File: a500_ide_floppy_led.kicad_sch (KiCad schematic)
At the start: 6 parts, among them J1 Motherboard, J2 Keyboard, J3 ~{IDE_ACTIVITY}, Q1 2N3906

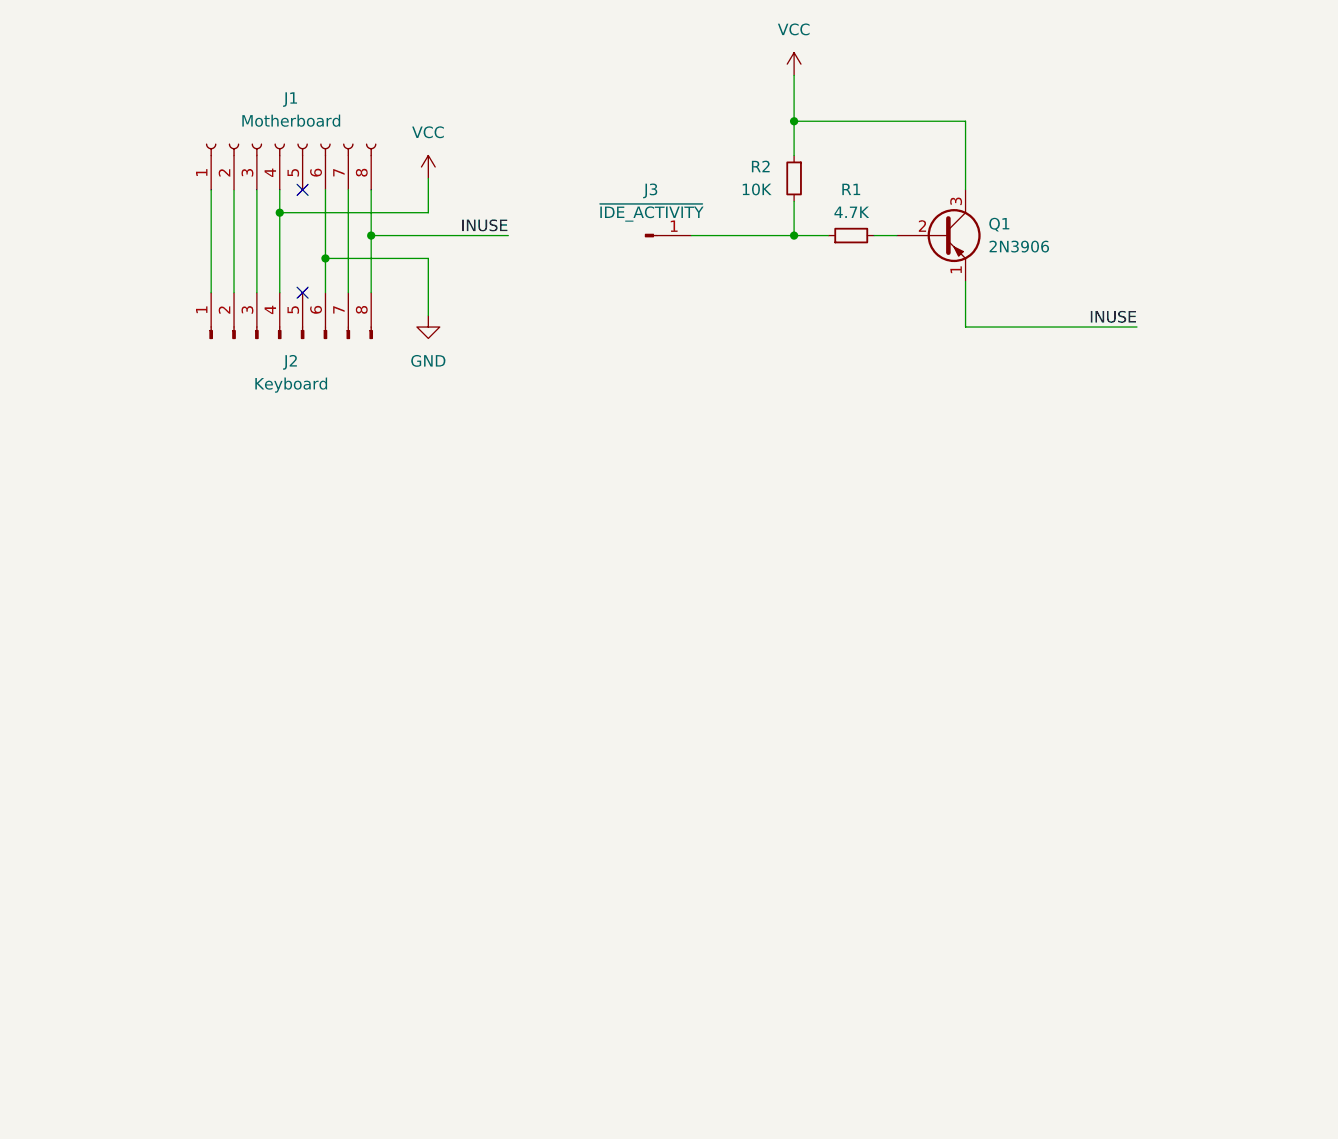
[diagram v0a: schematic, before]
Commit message: Add untested rev.1 that buffers the signal
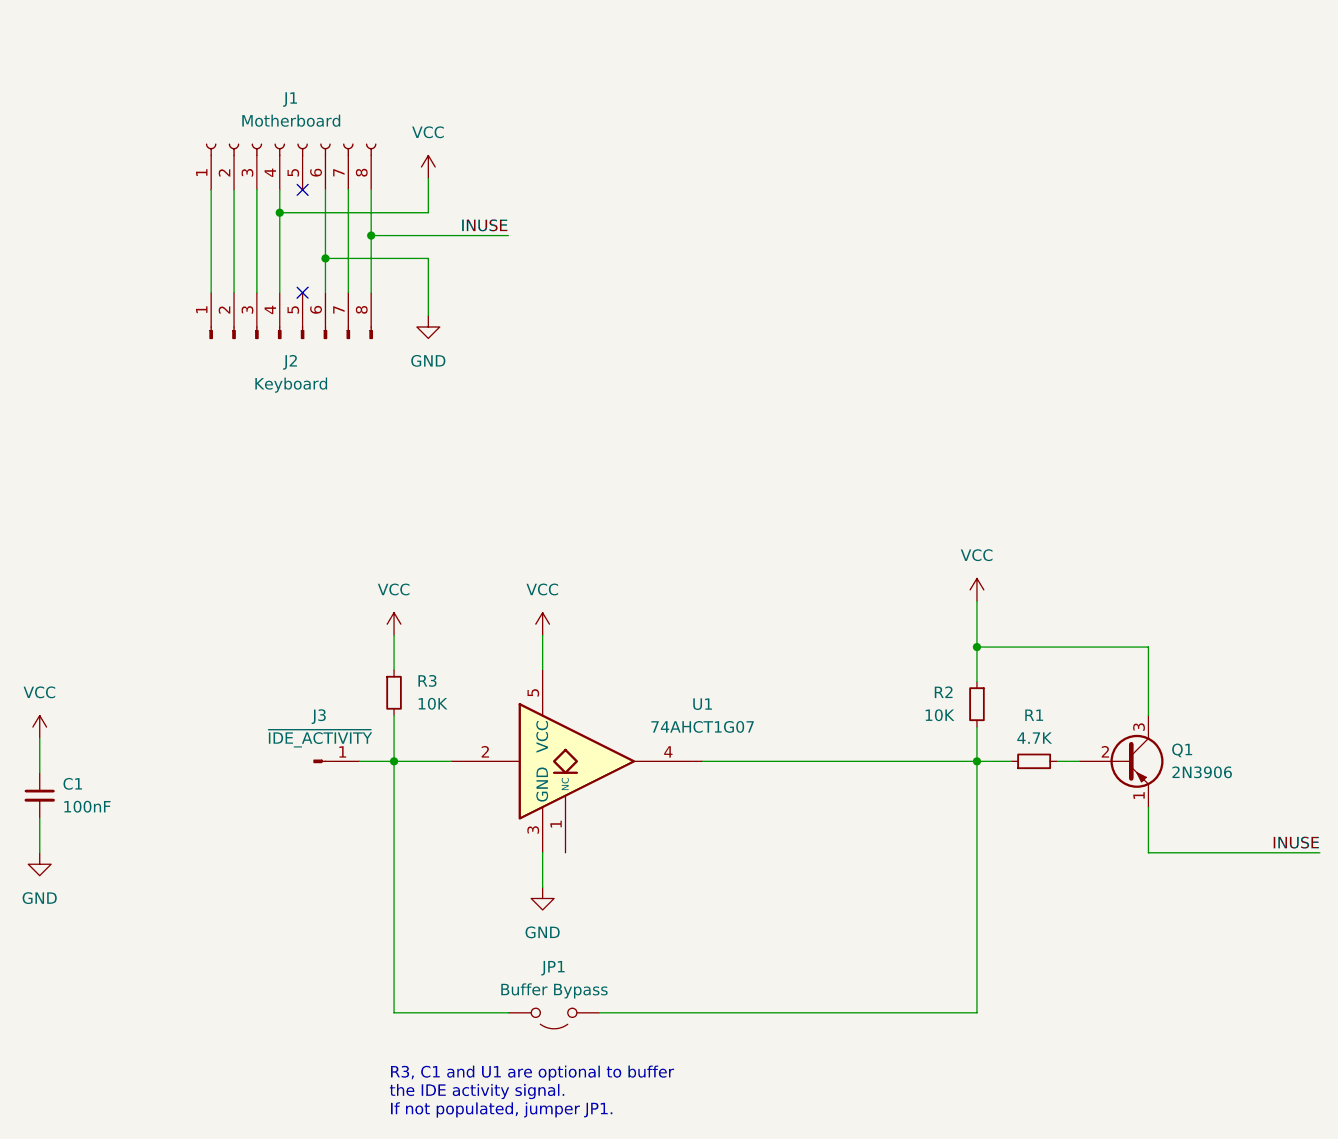
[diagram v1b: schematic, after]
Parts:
- added C1: 100nF, Capacitor_SMD:C_0805_2012Metric_Pad1.18x1.45mm_HandSolder, symbol Device:C_Small
- added JP1: Buffer Bypass, Jumper:SolderJumper-2_P1.3mm_Open_RoundedPad1.0x1.5mm, symbol Jumper:Jumper_2_Open
- added R3: 10K, Resistor_SMD:R_0805_2012Metric_Pad1.20x1.40mm_HandSolder, symbol Device:R_Small
- added U1: 74AHCT1G07, Package_TO_SOT_SMD:SOT-353_SC-70-5_Handsoldering, symbol 74xGxx:74LVC1G07
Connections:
- net GND: now also C1.2, U1.3 (GND)
- net VCC: now also C1.1, R3.1, U1.5 (VCC)
- net at R1.1, R2.2: now also JP1.1 (A), U1.4; no longer J3.1 (Pin_1)
- new net: J3.1 (Pin_1), JP1.2 (B), R3.2, U1.2
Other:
- note added: "R3, C1 and U1 are optional to buffer the IDE activity signal. If not populated, jumper JP1."
- moved on the sheet: J3, Q1, R1, R2
